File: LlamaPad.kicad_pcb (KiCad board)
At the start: 2 copper layers, 3.6 x 3.3 mm, 54 parts, among them J1 Conn_01x04_Pin, SW1 SW_Push, SW10 SW_Push, SW11 SW_Push, SW12 SW_Push, SW13 SW_Push, SW14 SW_Push, SW15 SW_Push, SW16 SW_Push, SW2 SW_Push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

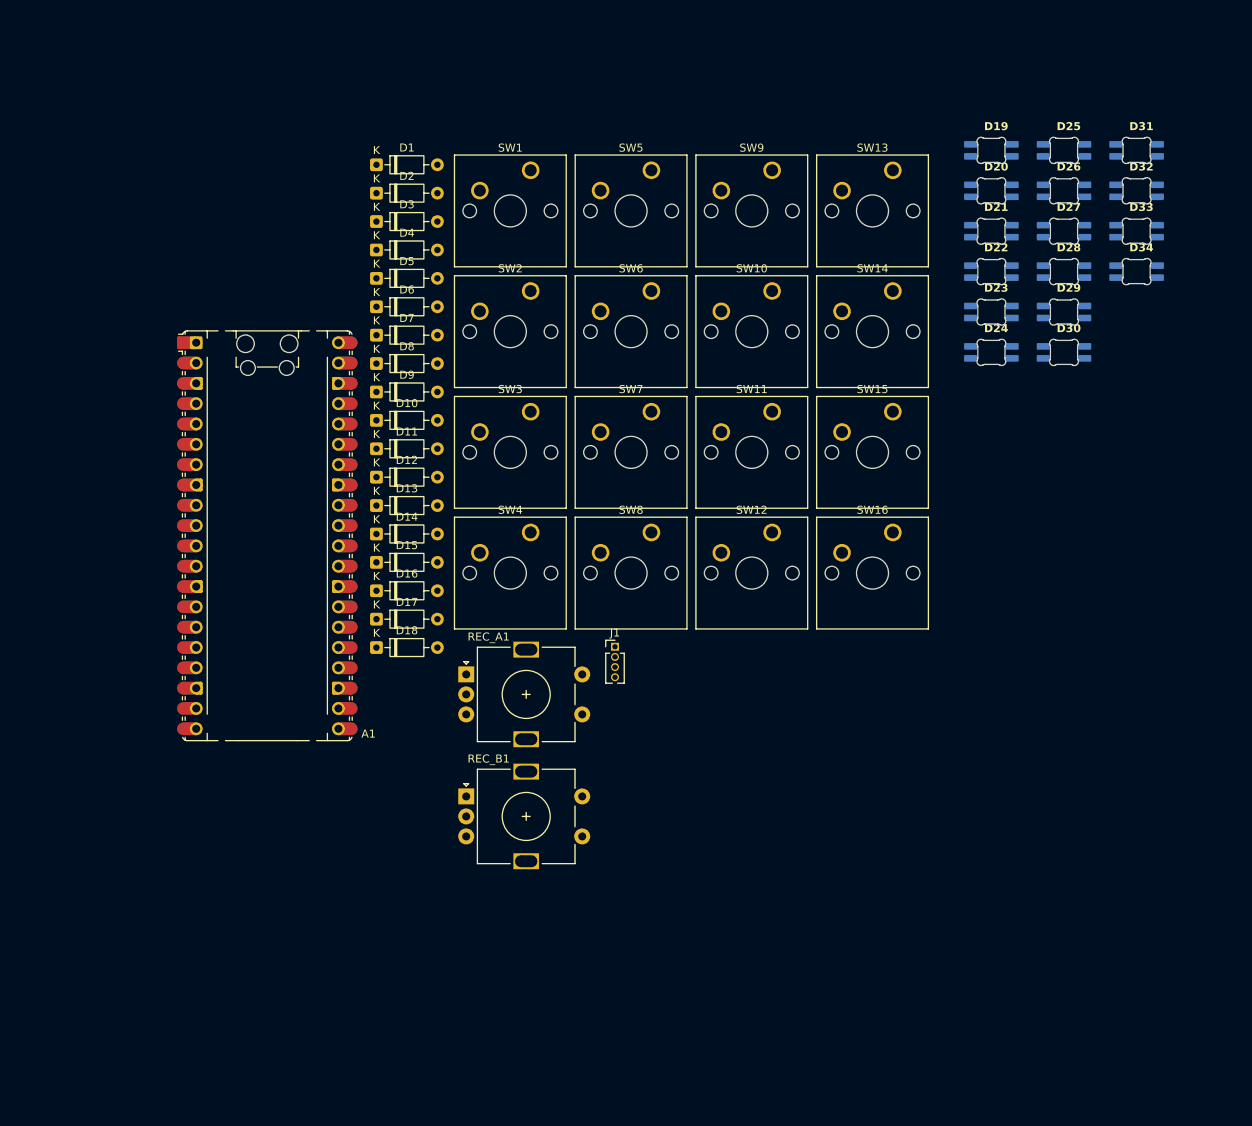
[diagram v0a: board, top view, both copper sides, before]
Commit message: feat: add edge cuts
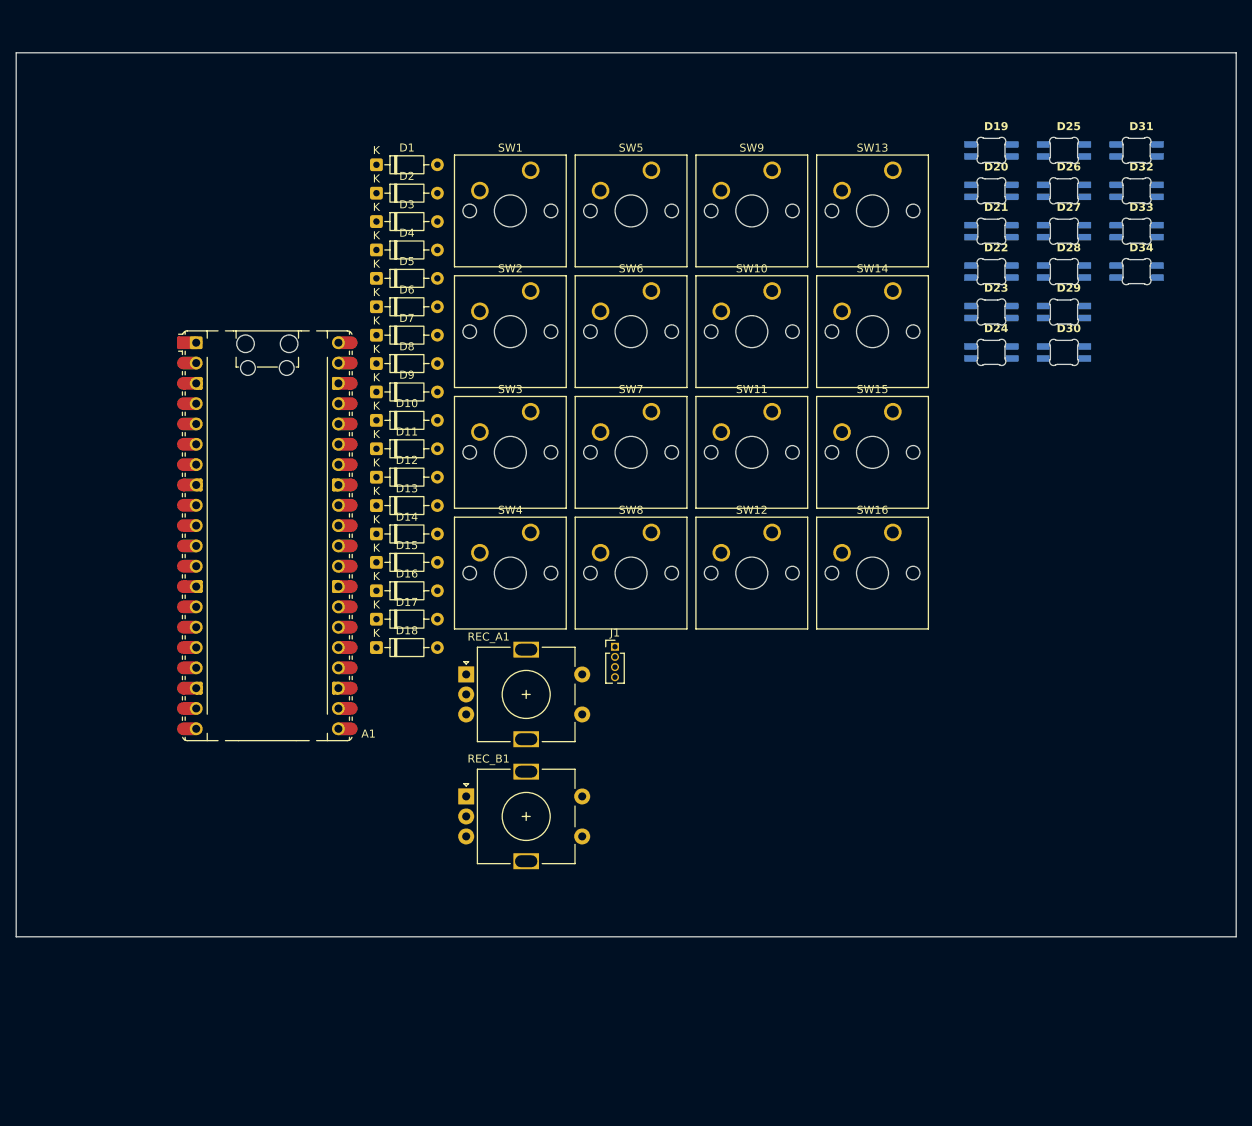
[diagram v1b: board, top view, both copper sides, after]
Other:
- board size 3.6 x 3.3 mm -> 152.5 x 110.5 mm
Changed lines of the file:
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@@
 		)
+	)
+	(gr_rect
+		(start 56.5 37)
+		(end 209 147.5)
+		(stroke
+			(width 0.05)
+			(type default)
+		)
+		(fill no)
+		(layer "Edge.Cuts")
 	)
 	(embedded_fonts no)

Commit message: feat: PCB rev1 (no traces)
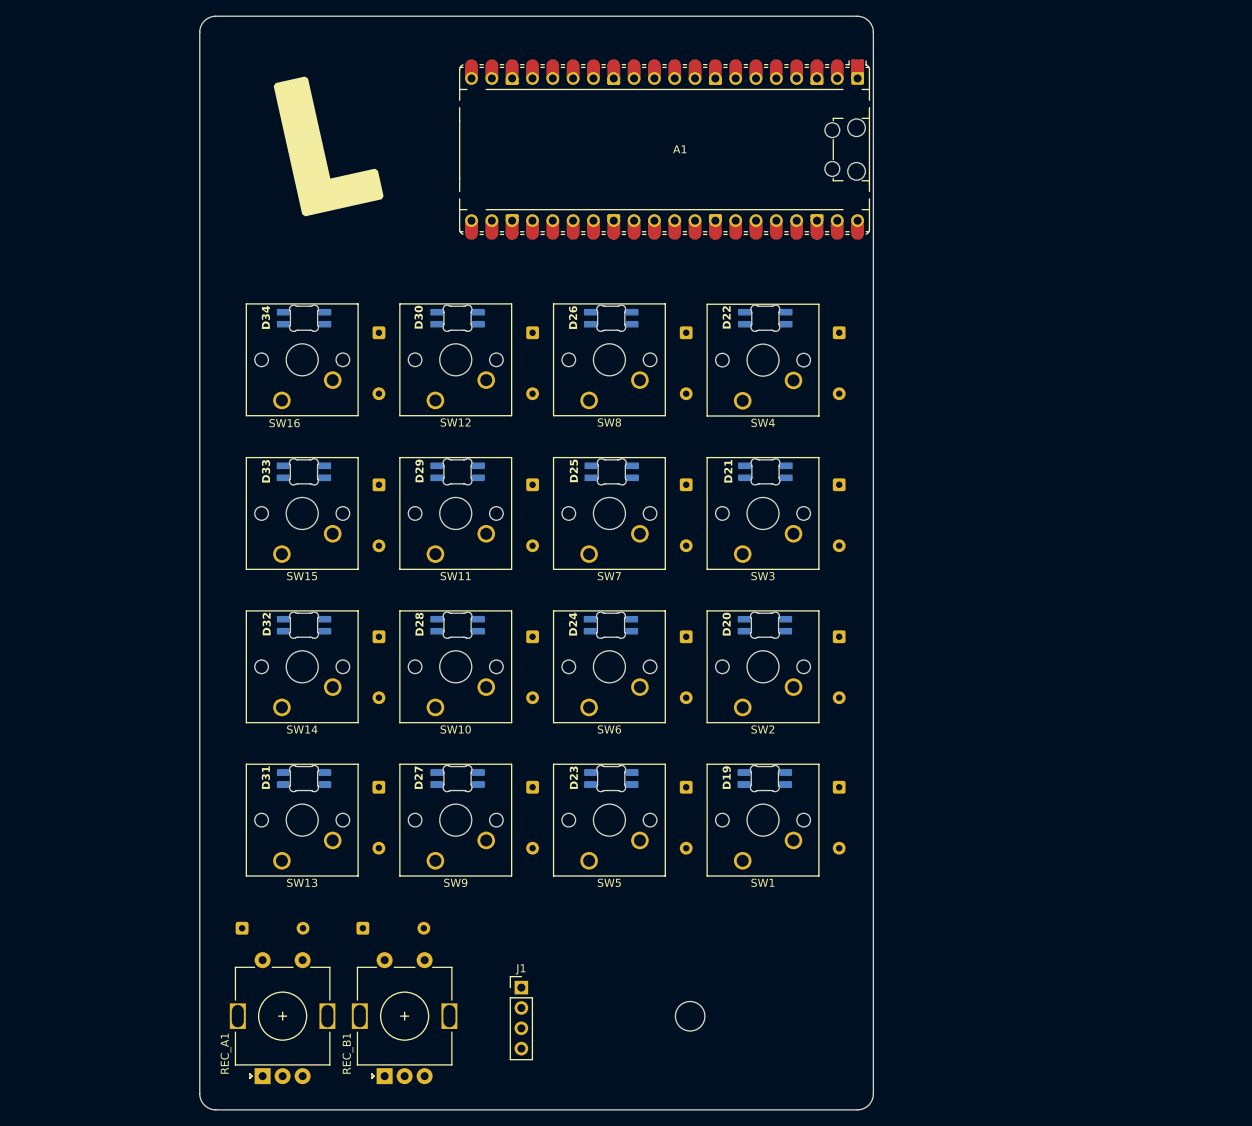
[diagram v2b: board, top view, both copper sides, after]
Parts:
- D1, D10, D11, D12, D13, D14, D15, D16, D17, D18, D2, D3, D4, D5, D6, D7, D8, D9: moved to B.Cu
- J1: footprint Connector_PinHeader_1.27mm:PinHeader_1x04_P1.27mm_Vertical -> Connector_PinHeader_2.54mm:PinHeader_1x04_P2.54mm_Vertical
- moved D31 130.2 mm to (92.5, 127.6), turned to 180 degrees
- moved D32 117.3 mm to (92.5, 108.4), turned to 180 degrees
- moved SW13 115.2 mm to (89.7, 138.0), turned to 180 degrees
- moved D33 108.3 mm to (92.5, 89.3), turned to 180 degrees
- moved D34 104.2 mm to (92.5, 70.1), turned to 180 degrees
- moved D27 102.0 mm to (111.7, 127.6), turned to 180 degrees
- moved SW9 96.0 mm to (108.9, 138.0), turned to 180 degrees
- moved SW14 92.4 mm to (89.7, 118.8), turned to 180 degrees
- moved SW1 90.3 mm to (147.3, 138.0), turned to 180 degrees
- moved D28 87.6 mm to (111.7, 108.4), turned to 180 degrees
- moved SW5 86.7 mm to (128.1, 138.0), turned to 180 degrees
- moved D19 83.3 mm to (150.1, 127.6), turned to 180 degrees
- moved SW15 78.4 mm to (89.7, 99.7), turned to 180 degrees
- moved D29 78.3 mm to (111.7, 89.3), turned to 180 degrees
- moved SW16 78.1 mm to (89.7, 80.5), turned to 180 degrees
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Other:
- board size 152.5 x 110.5 mm -> 84.2 x 136.7 mm
- board text added: "JLCJLCJLCJLC"

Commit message: feat: footprint stuff
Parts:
- added G***: LOGO, LOGO, B.Cu at (136.0, 50.0)

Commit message: feat: route the pcb and change schematic to be easier
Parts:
- D19, D20, D21, D22, D23, D24, D25, D26, D27, D28, D29, D30, D31, D32, D33, D34: footprint HackPad:SK6812MINI-E_fixed -> Llama_Other:SK6812MINI-E_fixed
- REC_A1, REC_B1: footprint HackPad:RotaryEncoder_Alps_EC11E-Switch_Vertical_H20mm -> RotaryEncoder:RotaryEncoder_Alps_EC11E-Switch_Vertical_H20mm
- SW1, SW10, SW11, SW12, SW13, SW14, SW15, SW16, SW2, SW3, SW4, SW5, SW6, SW7, SW8, SW9: footprint Button_Switch_Keyboard:SW_Cherry_MX_1.00u_PCB -> Switch_MX_Hotswap:MX-Hotswap-1U; moved to B.Cu
- moved SW13 60.3 mm to (149.8, 133.0), turned to 0 degrees
- moved SW14 60.3 mm to (149.8, 113.8), turned to 0 degrees
- moved SW15 60.3 mm to (149.8, 94.7), turned to 0 degrees
- moved SW16 60.3 mm to (149.8, 75.5), turned to 0 degrees
- moved SW1 55.3 mm to (92.2, 133.0), turned to 0 degrees
- moved SW2 55.3 mm to (92.2, 113.8), turned to 0 degrees
- moved SW3 55.3 mm to (92.2, 94.7), turned to 0 degrees
- moved SW4 55.3 mm to (92.2, 75.5), turned to 0 degrees
- moved SW10 22.3 mm to (130.6, 113.8), turned to 0 degrees
- moved SW12 22.3 mm to (130.6, 75.5), turned to 0 degrees
- moved SW9 22.3 mm to (130.6, 133.0), turned to 0 degrees
- moved SW11 22.3 mm to (130.6, 94.7), turned to 0 degrees
- moved D13 18.7 mm to (146.2, 85.2), turned to 0 degrees
- moved D14 18.7 mm to (146.2, 104.2), turned to 0 degrees
- moved D15 18.7 mm to (146.2, 123.2), turned to 0 degrees
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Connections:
- A1 pad 1: ROW0 -> unconnected-(A1-GPIO0-Pad1)
- A1 pad 10: COL3 -> unconnected-(A1-GPIO7-Pad10)
- A1 pad 11: COL4 -> unconnected-(A1-GPIO8-Pad11)
- A1 pad 12: REC_A1 -> unconnected-(A1-GPIO9-Pad12)
- A1 pad 15: REC_B1 -> REC_A1
- A1 pad 16: REC_B2 -> REC_B1
- A1 pad 17: ARGB_DATA -> REC_B2
- A1 pad 2: ROW1 -> unconnected-(A1-GPIO1-Pad2)
- A1 pad 21: unconnected-(A1-GPIO16-Pad21) -> COL0
- A1 pad 22: unconnected-(A1-GPIO17-Pad22)_1 -> COL1
- A1 pad 24: unconnected-(A1-GPIO18-Pad24)_1 -> COL2
- A1 pad 25: unconnected-(A1-GPIO19-Pad25) -> COL3
- A1 pad 26: unconnected-(A1-GPIO20-Pad26) -> COL4
- A1 pad 27: unconnected-(A1-GPIO21-Pad27) -> ROW1
- A1 pad 29: unconnected-(A1-GPIO22-Pad29)_1 -> ROW2
- A1 pad 31: unconnected-(A1-GPIO26_ADC0-Pad31) -> ROW3
- A1 pad 32: unconnected-(A1-GPIO27_ADC1-Pad32)_1 -> ROW0
- A1 pad 34: unconnected-(A1-GPIO28_ADC2-Pad34)_1 -> ARGB_DATA
- A1 pad 4: ROW2 -> unconnected-(A1-GPIO2-Pad4)
- A1 pad 5: ROW3 -> unconnected-(A1-GPIO3-Pad5)
- A1 pad 6: COL0 -> unconnected-(A1-GPIO4-Pad6)
- A1 pad 7: COL1 -> unconnected-(A1-GPIO5-Pad7)
- A1 pad 9: COL2 -> unconnected-(A1-GPIO6-Pad9)
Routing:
- net VCC: track 0.00 -> 383.1 mm, vias 0 -> 1
- net ROW1: track 0.00 -> 204.3 mm, vias 0 -> 2
- net OLED_SCL: track 0.00 -> 197.1 mm
- net COL4: track 0.00 -> 196.0 mm, vias 0 -> 1
- net OLED_SDA: track 0.00 -> 192.9 mm, vias 0 -> 1
- net REC_B1: track 0.00 -> 184.9 mm
- net ROW0: track 0.00 -> 183.7 mm, vias 0 -> 1
- net REC_A2: track 0.00 -> 174.6 mm
- net REC_B2: track 0.00 -> 173.4 mm
- net REC_A1: track 0.00 -> 171.7 mm
- net ROW3: track 0.00 -> 115.0 mm, vias 0 -> 2
- net ROW2: track 0.00 -> 114.1 mm, vias 0 -> 1
- net COL3: track 0.00 -> 113.0 mm, vias 0 -> 4
- net ARGB_DATA: track 0.00 -> 97.6 mm, vias 0 -> 4
- net COL2: track 0.00 -> 95.4 mm, vias 0 -> 4
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- added copper zone on B.Cu, net GND
- added copper zone on F.Cu, net GND
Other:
- board size 84.2 x 136.7 mm -> 84.7 x 136.7 mm
